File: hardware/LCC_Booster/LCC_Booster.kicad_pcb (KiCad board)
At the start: 2 copper layers, 115 x 100 mm, 92 parts, among them J1 A00-216-262-450, J2 54-00166, J3 Screw_Terminal_01x08, J4 Screw_Terminal_01x02, J5 Screw_Terminal_01x02, Q1 AO3400A, Q2 AO3400A, Q3 AO3400A, Q4 AO3400A, SW1 SW_Push, SW2 SW_Slide_DPDT, U1 ACPL-214-500E, U10 7410, U11 DRV8874PWPR, U12 7410, U13 7410, U14 7410, U15 7410, U16 DRV8874PWPR, U17 7410, U18 7410, U19 7410, U2 7410, U20 7410, U21 DRV8874PWPR, U22 MCP2515-xSO, U23 MCP2562-E-SN, U3 7410, U4 7410, U5 7410, U6 DRV8874PWPR, U7 7410, U8 7410, U9 7410, Y1 16.0 MHz, 22pF

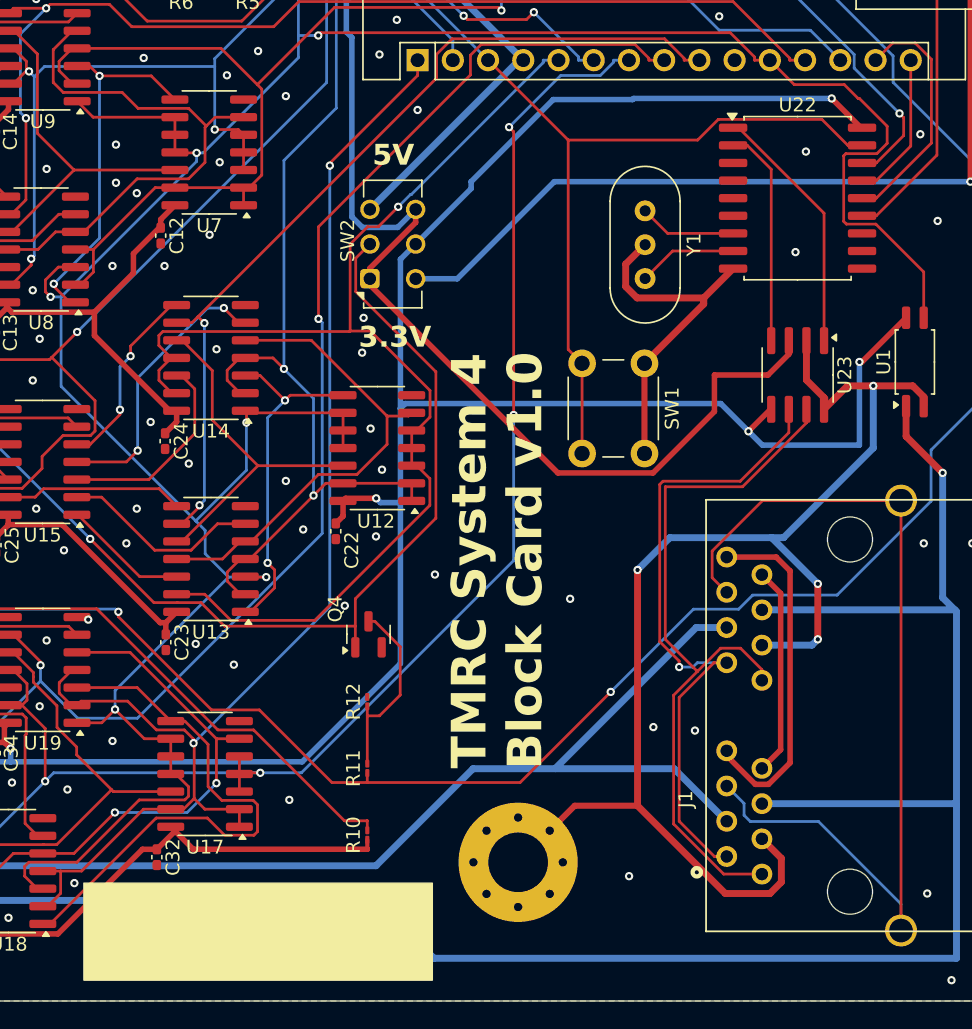
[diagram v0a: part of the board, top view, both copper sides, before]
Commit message: Regenerate LCC Booster Gerbers with More Power Filtering
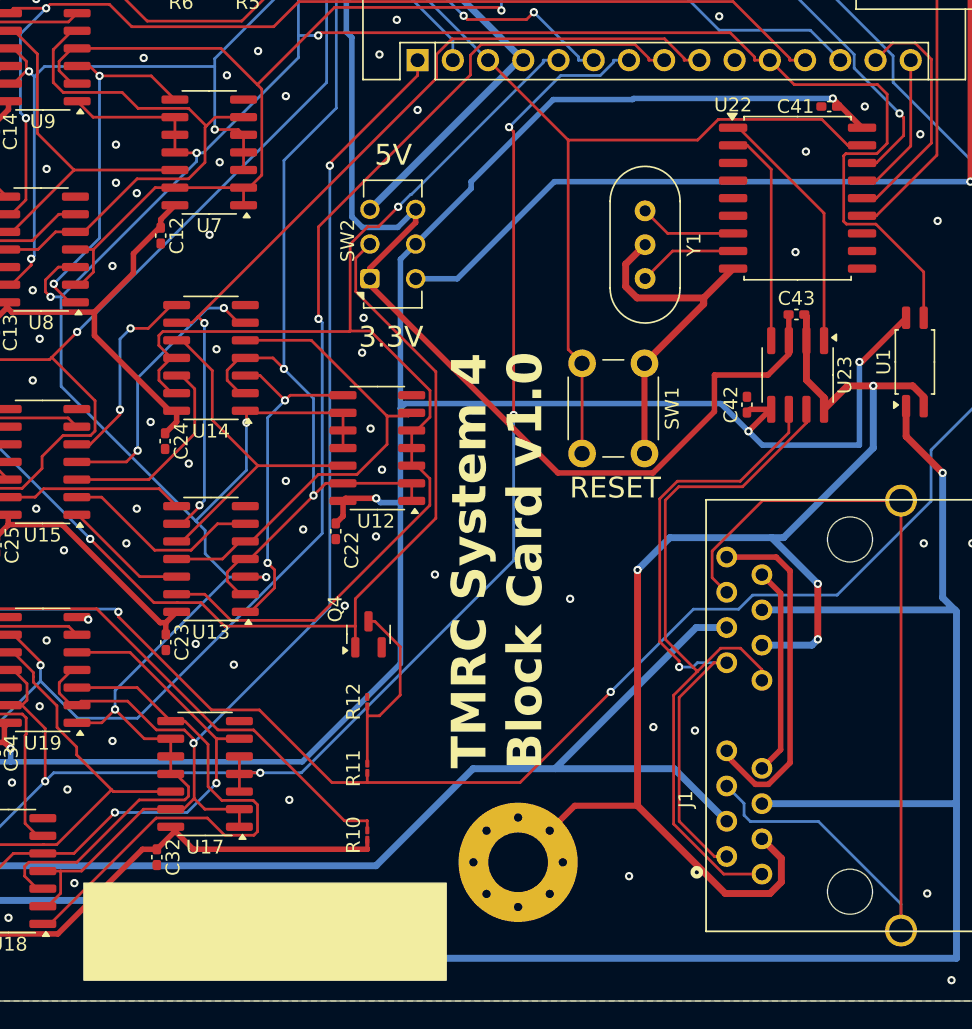
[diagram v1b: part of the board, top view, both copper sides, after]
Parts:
- added C41: C100n, Capacitor_SMD:C_0402_1005Metric_Pad0.74x0.62mm_HandSolder, F.Cu at (122.4, 55.5)
- added C42: C100n, Capacitor_SMD:C_0402_1005Metric_Pad0.74x0.62mm_HandSolder, F.Cu at (116.5, 77.0)
- added C43: C100n, Capacitor_SMD:C_0402_1005Metric_Pad0.74x0.62mm_HandSolder, F.Cu at (120.1, 70.5)
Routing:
- net GND: track 419.0 -> 420.9 mm
- net +5V: track 89.1 -> 91.0 mm
- net IOREF: track 565.0 -> 566.8 mm
- net /dcc_p: track 243.3 -> 244.7 mm
- net Net-(U14-Pad8): track 13.8 -> 14.5 mm
- net /can_l: track 48.1 -> 47.4 mm
- net /can_h: track 53.7 -> 53.1 mm
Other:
- board text added: "RESET"

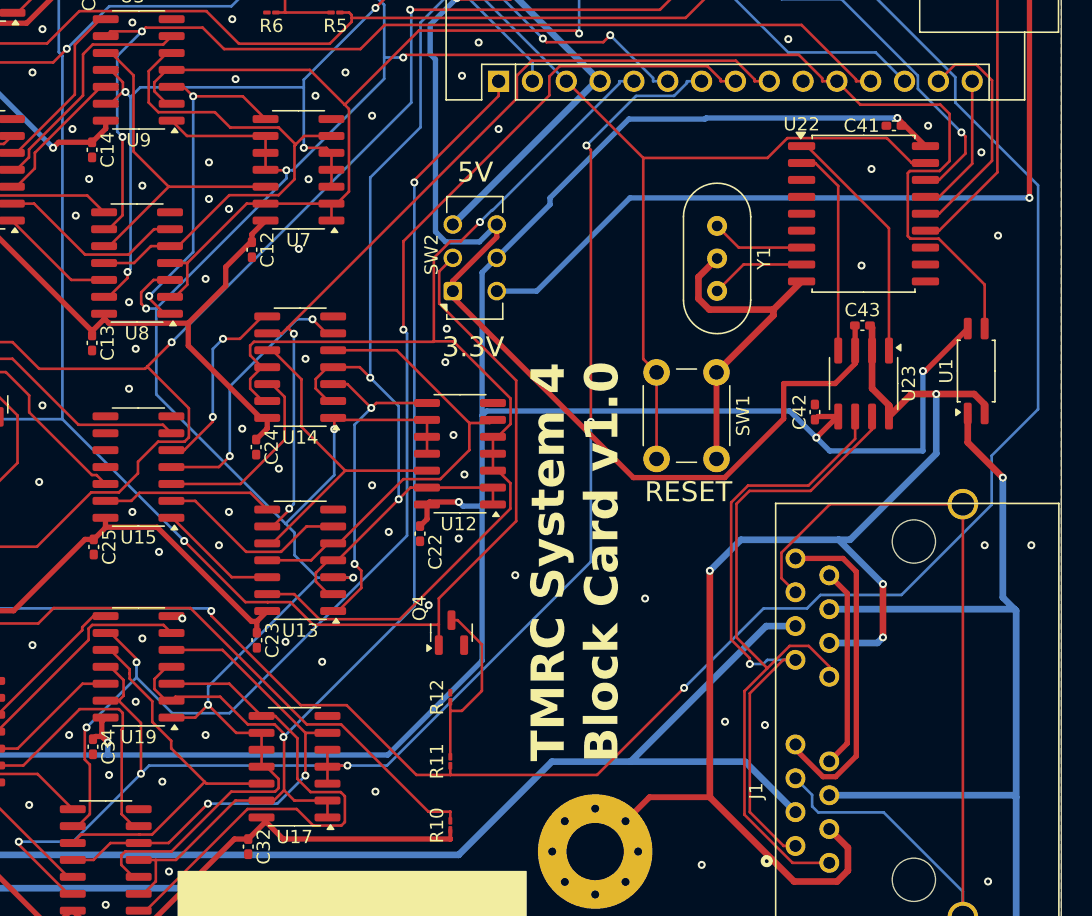
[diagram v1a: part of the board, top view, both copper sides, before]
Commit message: Start to work on code structure and added MCP2515 interrupt
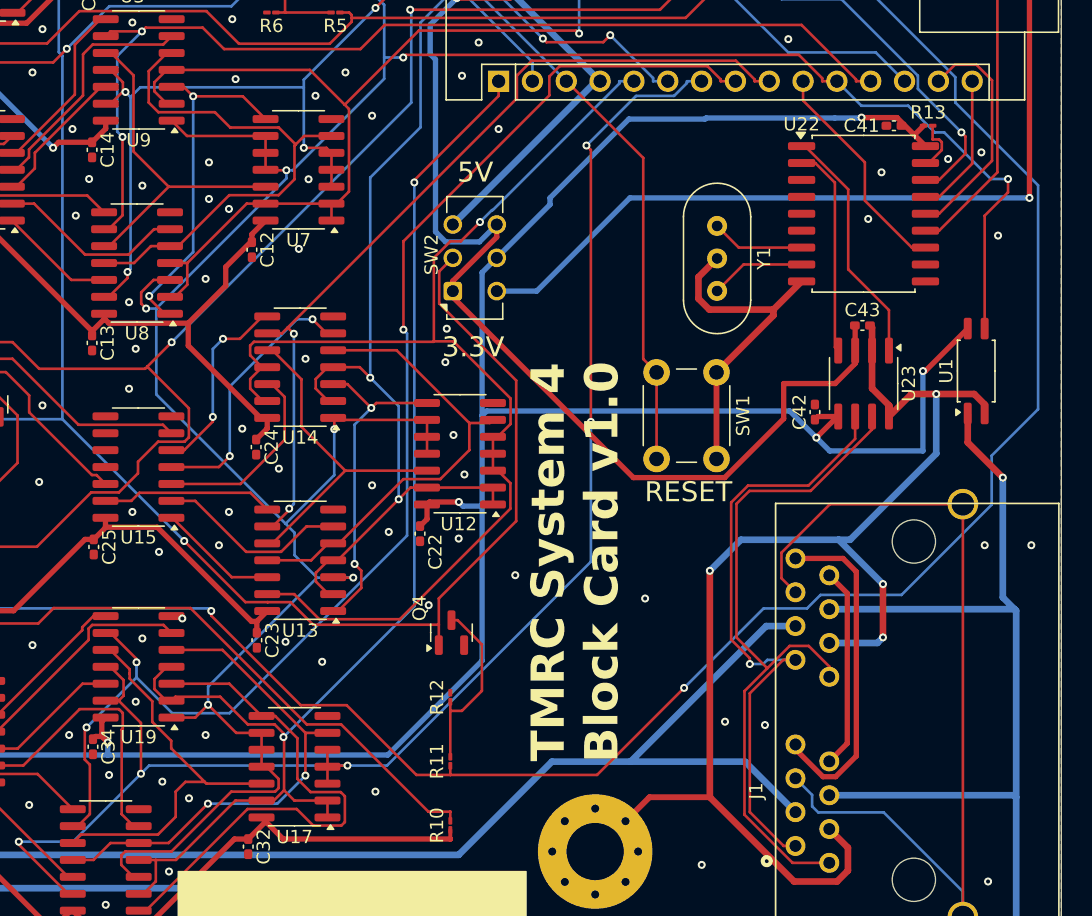
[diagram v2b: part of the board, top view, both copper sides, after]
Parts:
- added R13: R10k, Resistor_SMD:R_01005_0402Metric_Pad0.57x0.30mm_HandSolder, F.Cu at (125.0, 55.5)
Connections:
- A1 pad 10: /~{led} -> /int
- U22 pad 12: unconnected-(U22-~{INT}-Pad12) -> /int
- U22 pad 17: /~{reset} -> Net-(U22-~{RESET})
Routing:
- net /~{reset}: track 76.2 -> 53.6 mm
- net /int: track 0.00 -> 16.9 mm
- net Net-(U22-~{RESET}): track 0.00 -> 4.38 mm
- net /dcc_p: track 244.7 -> 240.7 mm, vias 7 -> 8
- net Net-(U17-Pad12): track 29.3 -> 30.4 mm
- net IOREF: track 566.8 -> 567.9 mm
- net GND: vias 125 -> 126

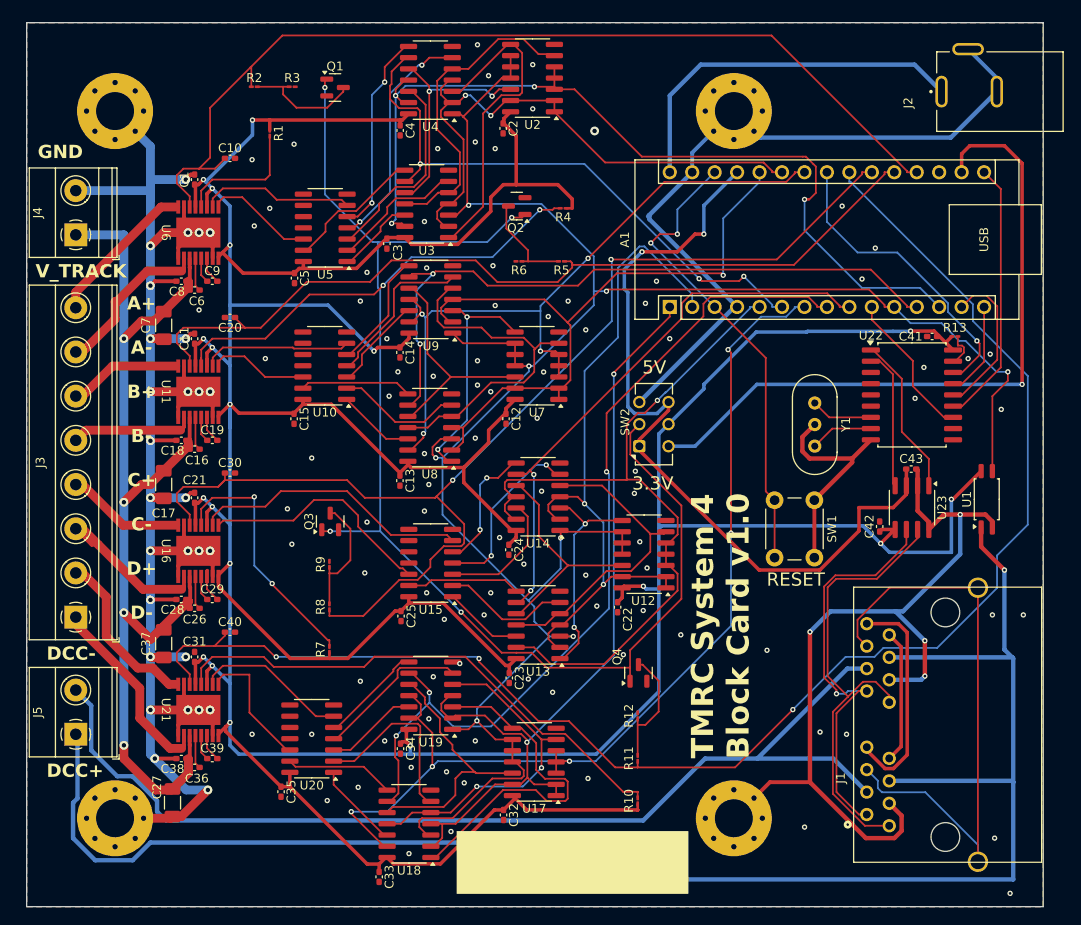
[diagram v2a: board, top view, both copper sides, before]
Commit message: Added MCP2515 Interrupt capability
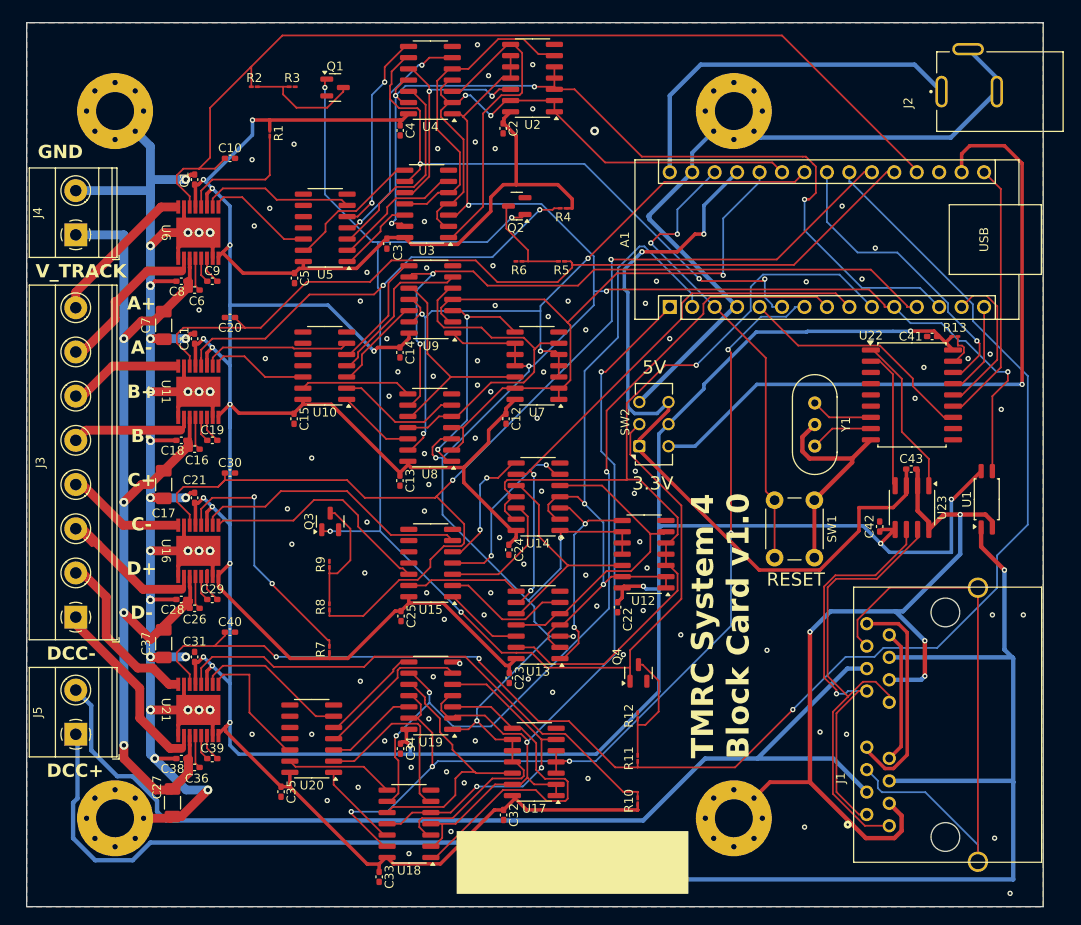
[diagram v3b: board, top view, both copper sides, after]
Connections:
- A1 pad 10: /int -> /dir_C
- A1 pad 5: /dir_C -> /int
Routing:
- net /dir_C: track 86.6 -> 105.2 mm
- net /int: track 16.9 -> 27.6 mm
- net /dcc_en_D: track 95.2 -> 96.7 mm
- net /pwm_A: track 66.8 -> 67.8 mm
- net GND: vias 126 -> 127

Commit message: Better Solder Jumpers, Better Pizza
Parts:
- removed R13: R10k, Resistor_SMD:R_01005_0402Metric_Pad0.57x0.30mm_HandSolder
- removed SW2: SW_Slide_DPDT, Button_Switch_THT:SW_CK_JS202011CQN_DPDT_Straight
- added C44: C22p, Capacitor_SMD:C_0402_1005Metric_Pad0.74x0.62mm_HandSolder, F.Cu at (107.5, 64.0)
- added C45: C22p, Capacitor_SMD:C_0402_1005Metric_Pad0.74x0.62mm_HandSolder, F.Cu at (107.5, 66.5)
- added JP1: SolderJumper_3_Bridged12, Jumper:SolderJumper-3_P1.3mm_Bridged12_RoundedPad1.0x1.5mm_NumberLabels, F.Cu at (91.0, 65.5)
- added JP2: SolderJumper_3_Bridged12, Jumper:SolderJumper-3_P1.3mm_Bridged12_RoundedPad1.0x1.5mm_NumberLabels, F.Cu at (94.5, 65.5)
- added JP3: SolderJumper_3_Bridged12, Jumper:SolderJumper-3_P1.3mm_Bridged12_RoundedPad1.0x1.5mm_NumberLabels, F.Cu at (112.5, 57.3)
- added JP4: SolderJumper_3_Bridged12, Jumper:SolderJumper-3_P1.3mm_Bridged12_RoundedPad1.0x1.5mm_NumberLabels, F.Cu at (109.0, 57.3)
- added JP5: SolderJumper_2_Open, Jumper:SolderJumper-2_P1.3mm_Open_RoundedPad1.0x1.5mm, F.Cu at (125.0, 79.0)
- U22: value MCP2515-xSO -> MCP2518FD-xQBB; footprint Package_SO:SOIC-18W_7.5x11.6mm_P1.27mm -> Package_SO:SOIC-14_3.9x8.7mm_P1.27mm
- Y1: value 16.0 MHz, 22pF -> ECS-400-20-46X; footprint Crystal:Crystal_HC49-U-3Pin_Vertical -> ECS_400_20_46X:XTAL_ECS-400-20-46X
- moved Y1 3.27 mm to (111.5, 65.3), turned to 90 degrees
- moved C41 2.54 mm to (122.0, 58.0)
- moved U22 2.14 mm to (118.4, 63.4)
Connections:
- A1 pad 13: /dir_A -> /cs_canrx
- A1 pad 23: /cs -> /dir_B
- A1 pad 24: /dir_B -> /dir_A
- A1 pad 5: /int -> /int_cantx
- U22 pad 10: unconnected-(U22-~{RX1BF}-Pad10) -> /sck
- U22 pad 11: unconnected-(U22-~{RX0BF}-Pad11) -> /copi
- U22 pad 12: /int -> /cipo
- U22 pad 13: /sck -> Net-(JP3-A)
- U22 pad 14: /copi -> IOREF
- U22 pad 4: unconnected-(U22-~{TX0RTS}-Pad4) -> Net-(JP4-A)
- U22 pad 5: unconnected-(U22-~{TX1RTS}-Pad5) -> Net-(U22-OSC2)
- U22 pad 6: unconnected-(U22-~{TX2RTS}-Pad6) -> Net-(U22-OSC1)
- U22 pad 7: Net-(U22-OSC2) -> GND
- U22 pad 8: Net-(U22-OSC1) -> unconnected-(U22-~{INT1}/GPIO1-Pad8)
- U22 pad 9: GND -> unconnected-(U22-~{INT0}/GPIO0/XSTBY-Pad9)
- Y1 pad 1: Net-(U22-OSC2) -> Net-(U22-OSC1)
- Y1 pad 2: GND -> Net-(U22-OSC2)
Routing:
- net /cs: track 34.3 -> 0.00 mm, vias 1 -> 0
- net /dir_A: track 102.2 -> 73.8 mm, vias 4 -> 3
- net /int: track 27.6 -> 0.00 mm
- net +5V: track 91.0 -> 108.2 mm, vias 2 -> 3
- net /cs_canrx: track 0.00 -> 15.7 mm
- net Net-(JP4-A): track 0.00 -> 11.9 mm
- net Net-(JP3-A): track 0.00 -> 11.0 mm
- net GND: track 420.9 -> 412.6 mm, vias 127 -> 130
- net /int_cantx: track 0.00 -> 8.22 mm
- net Net-(JP4-B): track 18.2 -> 26.0 mm, vias 0 -> 2
- net IOREF: track 567.9 -> 575.4 mm, vias 19 -> 20
- net /can_shield: track 68.0 -> 73.4 mm
- net /sck: track 30.1 -> 34.9 mm
- net /copi: track 17.7 -> 22.2 mm
- net /cipo: track 10.7 -> 15.1 mm
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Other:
- board text added: "CAN"
- board text added: "SPI"
